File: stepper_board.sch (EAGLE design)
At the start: 59 parts, among them IC1 MCP1703DB, U2 MIC2005A-1YM5, Y1 12 MHz

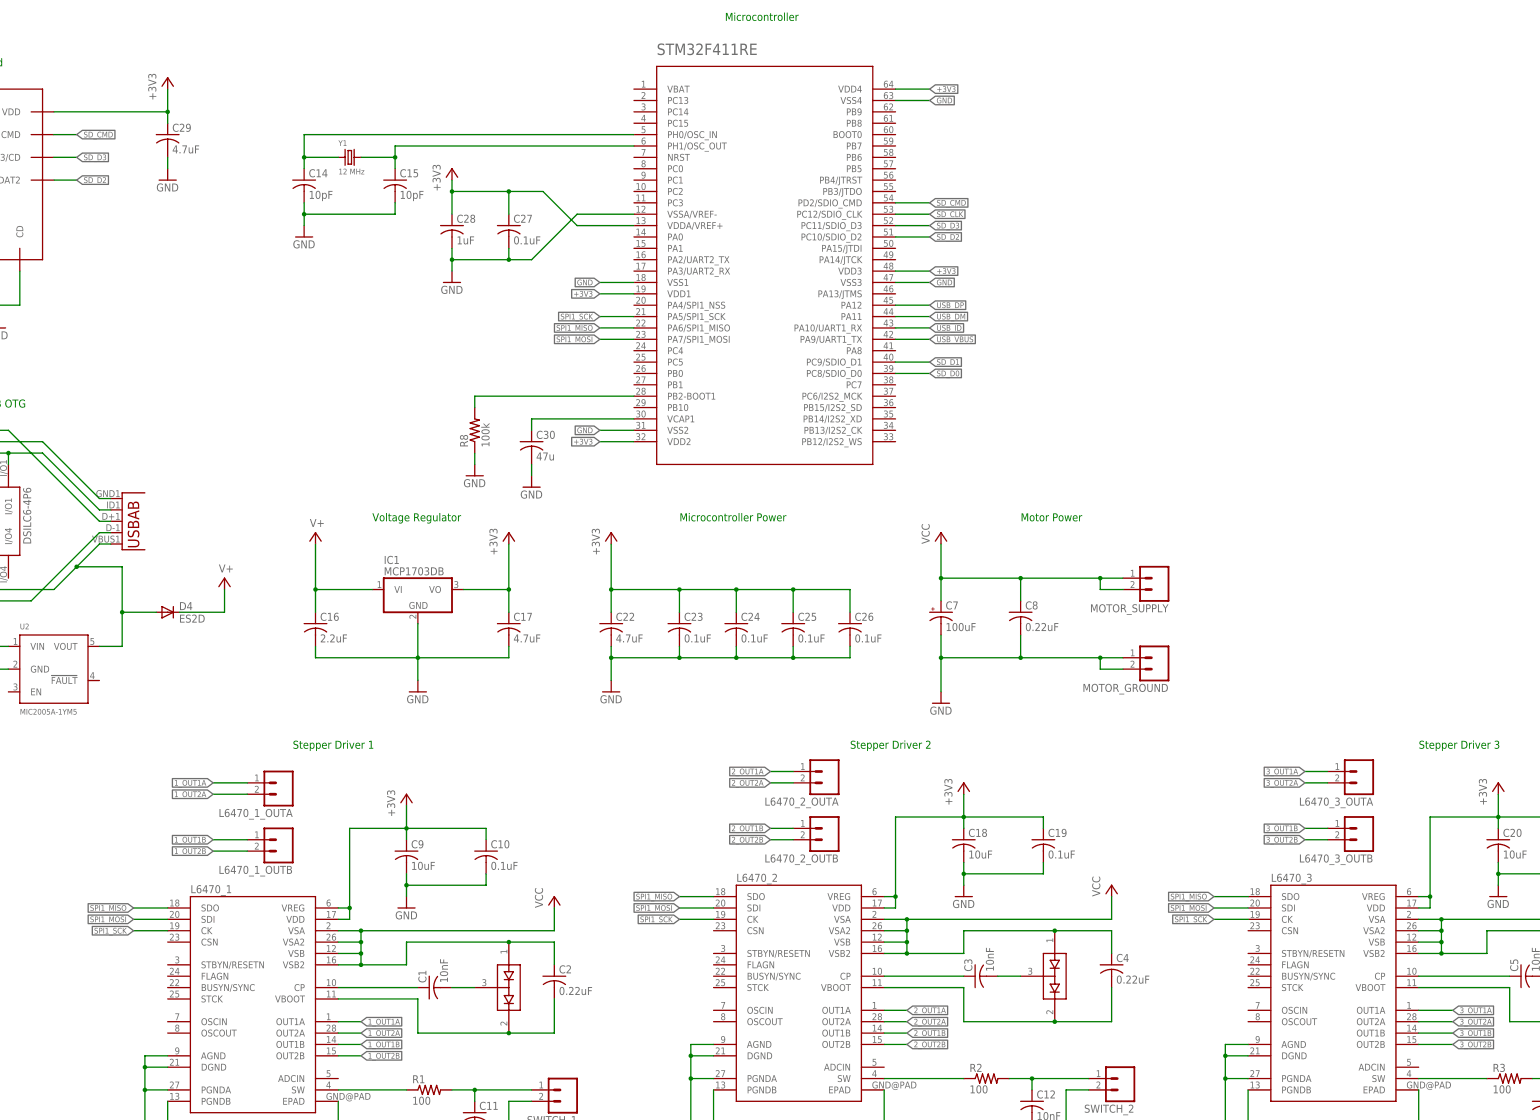
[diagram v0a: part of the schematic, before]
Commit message: Tried to start unraveling the rats' nest.
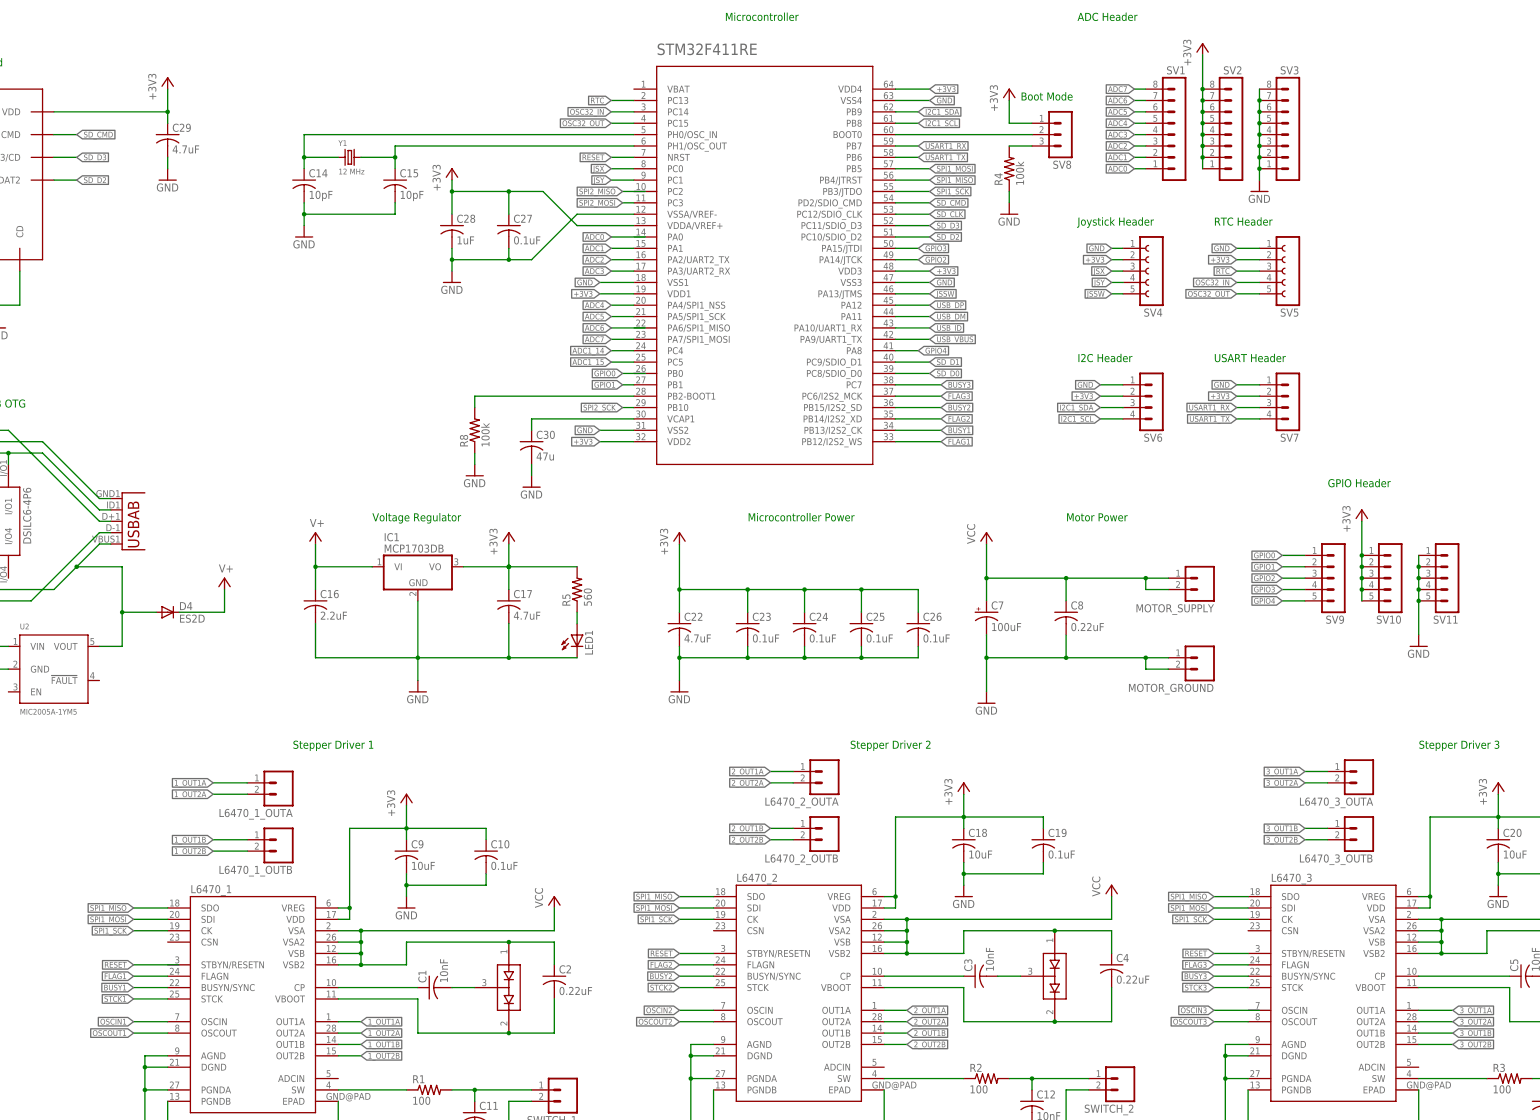
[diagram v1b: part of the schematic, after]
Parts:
- added LED1: (no value), led:LEDCHIP-LED0805
- added R4: 100k, rcl:R-US_R0805
- added R5: 560, rcl:R-US_R0805
- added SV1, SV2, SV3: (no value), con-lstb:MA08-1
- added SV10, SV11, SV9: (no value), con-lstb:MA05-1
- added SV4, SV5: (no value), con-lsta:FE05-1
- added SV6, SV7: (no value), con-lstb:MA04-1
- added SV8: (no value), con-lstb:MA03-1
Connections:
- new net ADC0: SV1.1
- new net ADC1: STM32F411RE.PA1, SV1.2
- new net ADC1_14: STM32F411RE.PC4
- new net ADC1_15: STM32F411RE.PC5
- new net ADC2: STM32F411RE.PA2/UART2_TX, SV1.3
- new net ADC3: STM32F411RE.PA3/UART2_RX, SV1.4
- new net ADC4: STM32F411RE.PA4/SPI1_NSS, SV1.5
- new net ADC5: STM32F411RE.PA5/SPI1_SCK, SV1.6
- new net ADC6: SV1.7
- new net ADC7: STM32F411RE.PA7/SPI1_MOSI, SV1.8
- new net BUSY1: L6470_1.BUSYN/SYNC, STM32F411RE.PB13/I2S2_CK
- new net BUSY2: L6470_2.BUSYN/SYNC, STM32F411RE.PB15/I2S2_SD
- new net BUSY3: L6470_3.BUSYN/SYNC, STM32F411RE.PC7
- new net FLAG1: L6470_1.FLAGN, STM32F411RE.PB12/I2S2_WS
- new net FLAG2: L6470_2.FLAGN, STM32F411RE.PB14/I2S2_XD
- new net FLAG3: L6470_3.FLAGN, STM32F411RE.PC6/I2S2_MCK
- new net GPIO0: SV9.1
- new net GPIO1: STM32F411RE.PB1, SV9.2
- new net GPIO2: STM32F411RE.PA14/JTCK, SV9.3
- new net GPIO3: STM32F411RE.PA15/JTDI, SV9.4
- new net GPIO4: STM32F411RE.PA8, SV9.5
- new net I2C1_SCL: STM32F411RE.PB8, SV6.4
- new net I2C1_SDA: STM32F411RE.PB9, SV6.3
- new net JSSW: STM32F411RE.PA13/JTMS, SV4.5
- new net JSX: STM32F411RE.PC0, SV4.3
- new net JSY: STM32F411RE.PC1, SV4.4
- new net N$18: STM32F411RE.BOOT0, SV8.2
- new net N$19: R4.2, SV8.3
- new net N$20: LED1.A, R5.1
- new net OSC32_IN: STM32F411RE.PC14, SV5.4
- new net OSC32_OUT: STM32F411RE.PC15, SV5.5
- new net OSCIN1: L6470_1.OSCIN
- new net OSCIN2: L6470_2.OSCIN
- new net OSCOUT1: L6470_1.OSCOUT
- new net OSCOUT2: L6470_2.OSCOUT
- new net OSCOUT3: L6470_3.OSCOUT
- new net RESET: L6470_2.STBYN/RESETN, L6470_3.STBYN/RESETN, STM32F411RE.NRST
- new net RTC: STM32F411RE.PC13, SV5.3
- new net SPI2_MOSI: STM32F411RE.PC3
- new net SPI2_SCK: STM32F411RE.PB10
- new net STCK1: L6470_1.STCK
- new net STCK2: L6470_2.STCK
- new net STCK3: L6470_3.STCK
- new net USART1_RX: STM32F411RE.PB7, SV7.3
- new net USART1_TX: STM32F411RE.PB6, SV7.4
- net +3V3: now also R5.2, SV10.1, SV10.2, SV10.3, SV10.4, SV10.5, SV2.1, SV2.2, SV2.3, SV2.4, SV2.5, SV2.6, SV2.7, SV2.8, SV4.2, SV5.2, SV6.2, SV7.2, SV8.1
- net GND: now also LED1.C, R4.1, SV11.1, SV11.2, SV11.3, SV11.4, SV11.5, SV3.1, SV3.2, SV3.3, SV3.4, SV3.5, SV3.6, SV3.7, SV3.8, SV4.1, SV5.1, SV6.1, SV7.1
- net SPI1_MISO: now also STM32F411RE.PB4/JTRST; no longer STM32F411RE.PA6/SPI1_MISO
- net SPI1_MOSI: now also STM32F411RE.PB5; no longer STM32F411RE.PA7/SPI1_MOSI
- net SPI1_SCK: now also STM32F411RE.PB3/JTDO; no longer STM32F411RE.PA5/SPI1_SCK
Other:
- note added: "ADC Header"
- note added: "Boot Mode"
- note added: "GPIO Header"
- note added: "I2C Header"
- note added: "Joystick Header"
- note added: "RTC Header"
- note added: "USART Header"
- moved on the sheet: C16, C17, C22, C23, C24, C25, C26, C7, C8, IC1, MOTOR_GROUND, MOTOR_SUPPLY

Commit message: More wiring in progress
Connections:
- net 3_OUT1A: now also L6470_3_OUTA.2; no longer L6470_3_OUTA.1
- net 3_OUT2A: now also L6470_3_OUTA.1; no longer L6470_3_OUTA.2
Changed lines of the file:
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@@
 </segment>
 <segment>
-<pinref part="L6470_3_OUTA" gate="G$1" pin="1"/>
-<wire x1="127" y1="-111.76" x2="121.92" y2="-111.76" width="0.1524" layer="91"/>
-<label x="121.92" y="-111.76" size="1.27" layer="95" rot="R180" xref="yes"/>
+<pinref part="L6470_3_OUTA" gate="G$1" pin="2"/>
+<wire x1="127" y1="-114.3" x2="121.92" y2="-114.3" width="0.1524" layer="91"/>
+<label x="121.92" y="-114.3" size="1.27" layer="95" rot="R180" xref="yes"/>
 </segment>
 </net>
@@
 </segment>
 <segment>
-<pinref part="L6470_3_OUTA" gate="G$1" pin="2"/>
-<wire x1="127" y1="-114.3" x2="121.92" y2="-114.3" width="0.1524" layer="91"/>
-<label x="121.92" y="-114.3" size="1.27" layer="95" rot="R180" xref="yes"/>
+<pinref part="L6470_3_OUTA" gate="G$1" pin="1"/>
+<wire x1="127" y1="-111.76" x2="121.92" y2="-111.76" width="0.1524" layer="91"/>
+<label x="121.92" y="-111.76" size="1.27" layer="95" rot="R180" xref="yes"/>
 </segment>
 </net>

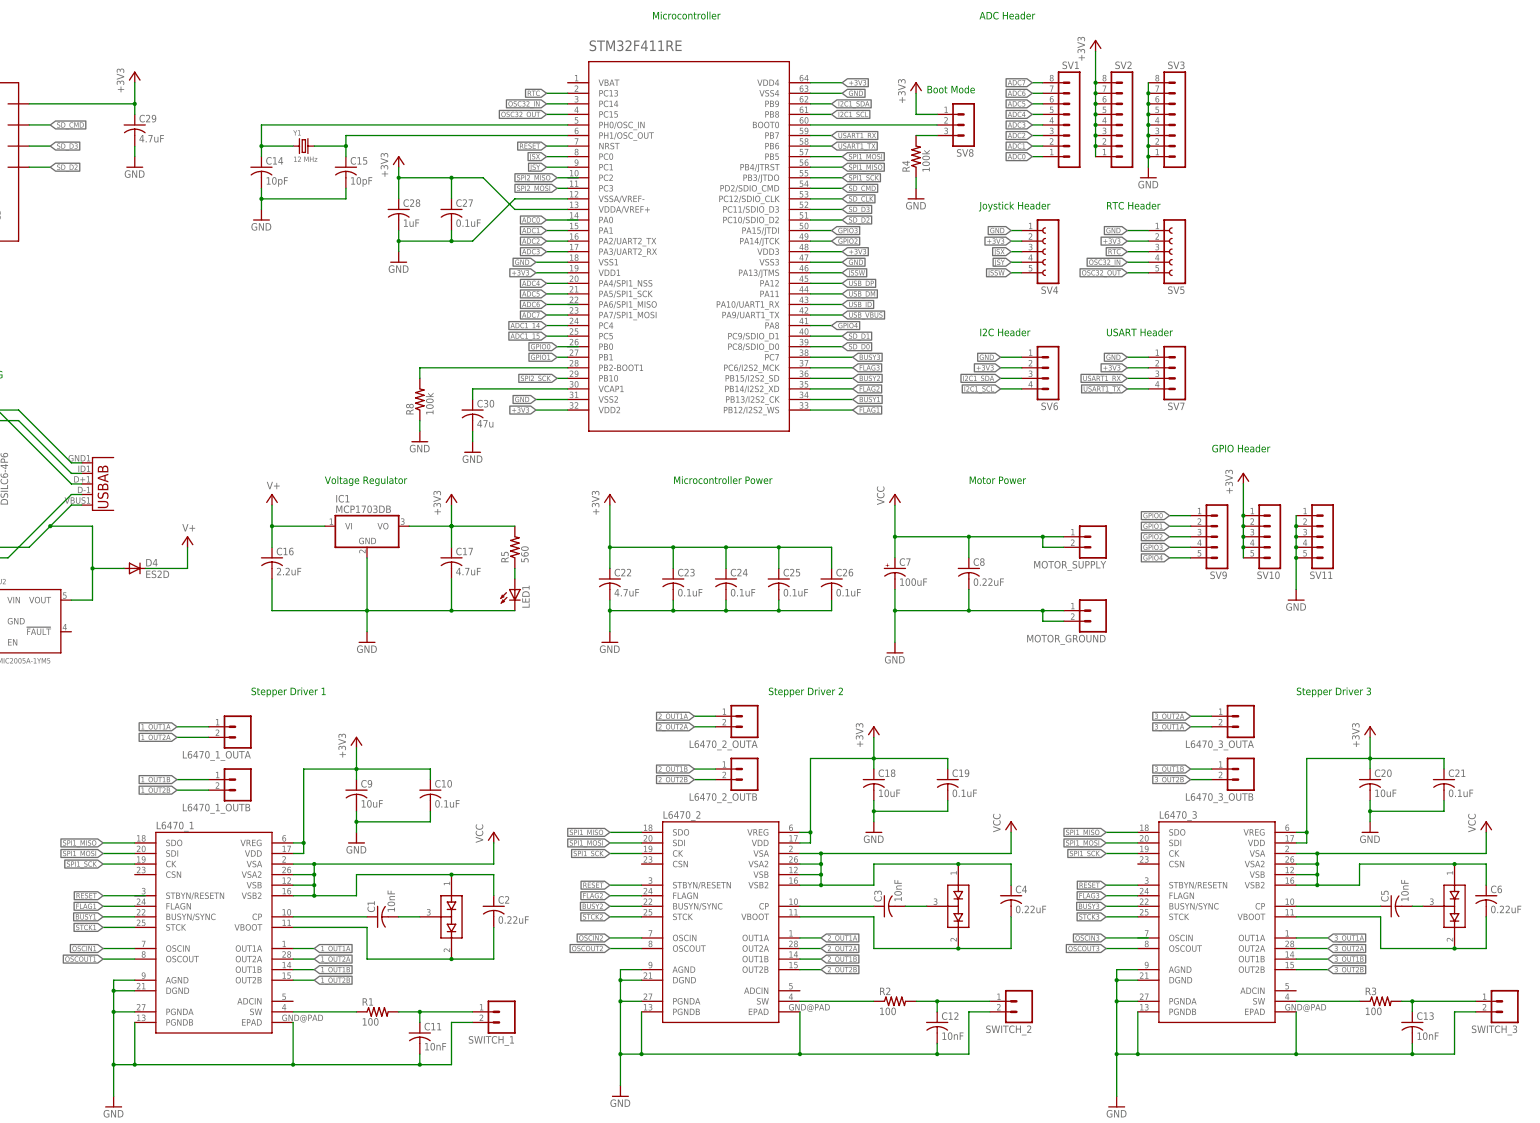
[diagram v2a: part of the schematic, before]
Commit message: Changed L6470 package footprint, added chip select pins to drivers, started routing
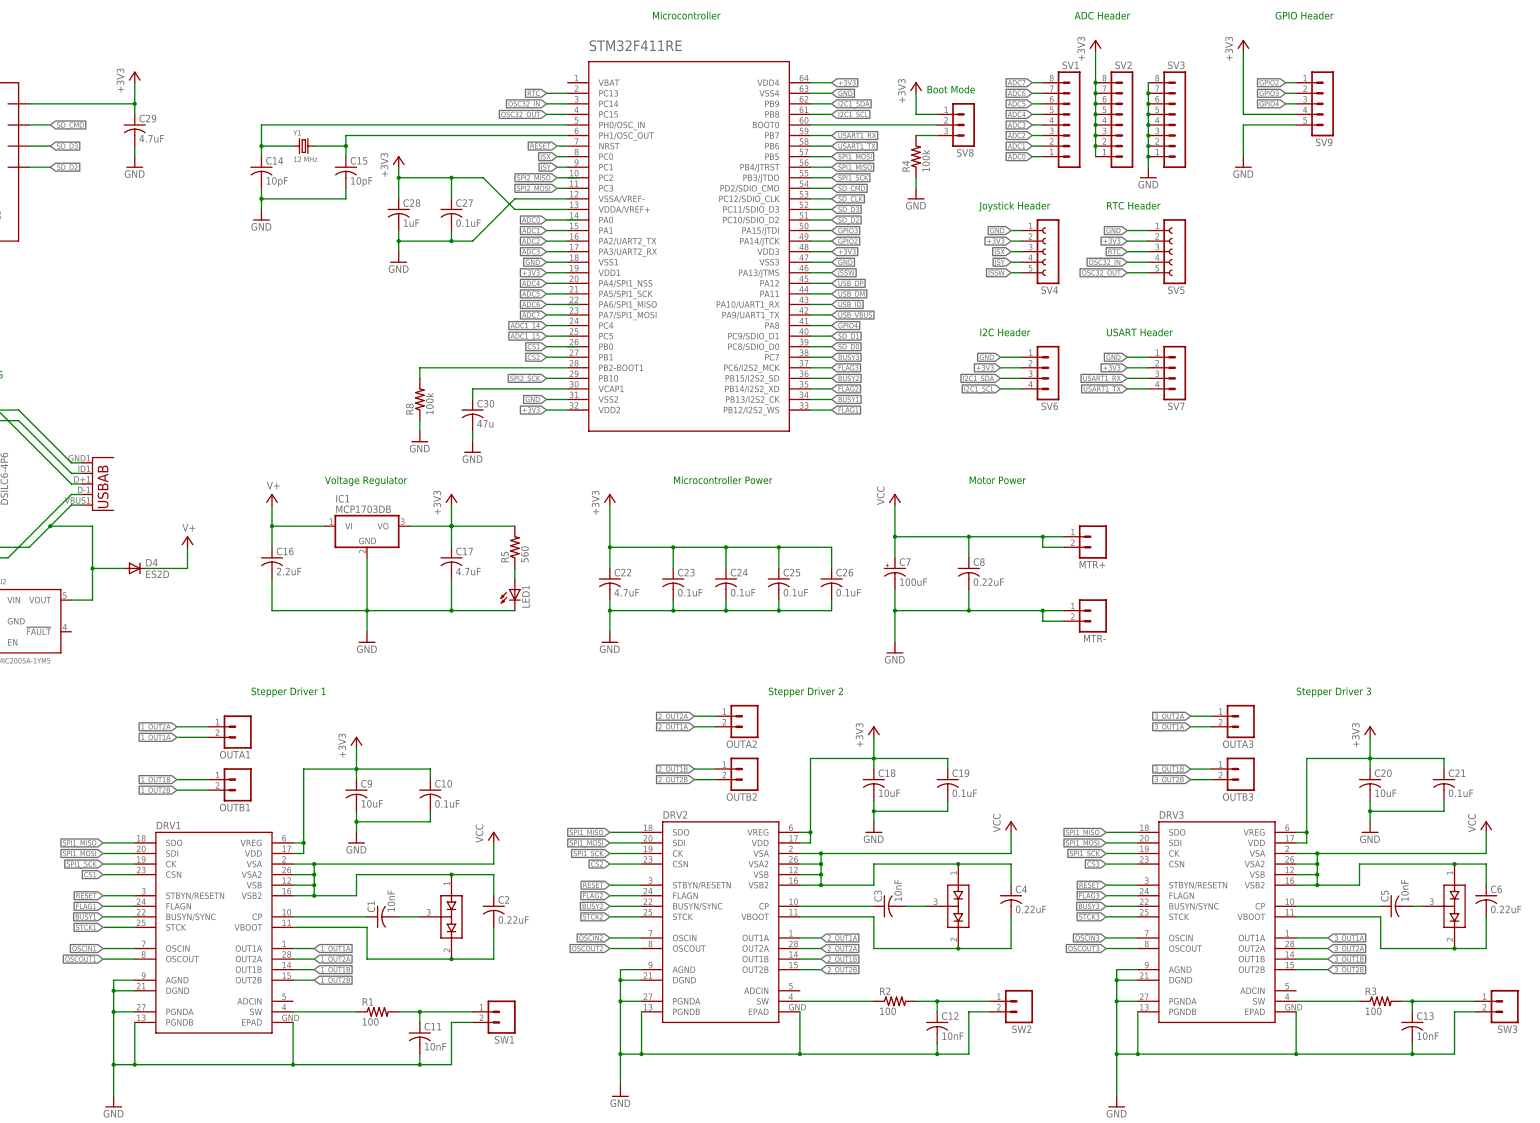
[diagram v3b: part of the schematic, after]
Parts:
- removed L6470_1, L6470_2, L6470_3: (no value), SparkFun-PowerIC:L6470
- removed SV10, SV11: (no value), con-lstb:MA05-1
- added DRV1, DRV2, DRV3: (no value), PowerIC_spark:L6470
- renumbered L6470_1_OUTA to OUTA1, L6470_1_OUTB to OUTB1, L6470_2_OUTA to OUTA2, L6470_2_OUTB to OUTB2, L6470_3_OUTA to OUTA3, L6470_3_OUTB to OUTB3, MOTOR_GROUND to MTR-, MOTOR_SUPPLY to MTR+, SWITCH_1 to SW1, SWITCH_2 to SW2, SWITCH_3 to SW3
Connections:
- removed net GPIO0: SV9.1
- removed net GPIO1: STM32F411RE.PB1, SV9.2
- new net CS1: DRV1.CSN
- new net CS2: DRV2.CSN, STM32F411RE.PB1
- new net CS3: DRV3.CSN
- new net OSCIN3: DRV3.OSCIN
- net +3V3: now also DRV1.VDD, DRV1.VREG, DRV2.VDD, DRV2.VREG, DRV3.VDD, DRV3.VREG, SV9.4; no longer L6470_1.VDD, L6470_1.VREG, L6470_2.VDD, L6470_2.VREG, L6470_3.VDD, L6470_3.VREG, SV10.1, SV10.2, SV10.3, SV10.4, SV10.5
- net 1_OUT1A: now also DRV1.OUT1A, OUTA1.2; no longer L6470_1.OUT1A, OUTA1.1
- net 1_OUT1B: now also DRV1.OUT1B; no longer L6470_1.OUT1B
- net 1_OUT2A: now also DRV1.OUT2A, OUTA1.1; no longer L6470_1.OUT2A, OUTA1.2
- net 1_OUT2B: now also DRV1.OUT2B; no longer L6470_1.OUT2B
- net 2_OUT1A: now also DRV2.OUT1A, OUTA2.2; no longer L6470_2.OUT1A, OUTA2.1
- net 2_OUT1B: now also DRV2.OUT1B; no longer L6470_2.OUT1B
- net 2_OUT2A: now also DRV2.OUT2A, OUTA2.1; no longer L6470_2.OUT2A, OUTA2.2
- net 2_OUT2B: now also DRV2.OUT2B; no longer L6470_2.OUT2B
- net 3_OUT1A: now also DRV3.OUT1A; no longer L6470_3.OUT1A
- net 3_OUT1B: now also DRV3.OUT1B; no longer L6470_3.OUT1B
- net 3_OUT2A: now also DRV3.OUT2A; no longer L6470_3.OUT2A
- net 3_OUT2B: now also DRV3.OUT2B; no longer L6470_3.OUT2B
- net BUSY1: now also DRV1.BUSYN/SYNC; no longer L6470_1.BUSYN/SYNC
- net BUSY2: now also DRV2.BUSYN/SYNC; no longer L6470_2.BUSYN/SYNC
- net BUSY3: now also DRV3.BUSYN/SYNC; no longer L6470_3.BUSYN/SYNC
- net FLAG1: now also DRV1.FLAGN; no longer L6470_1.FLAGN
- net FLAG2: now also DRV2.FLAGN; no longer L6470_2.FLAGN
- net FLAG3: now also DRV3.FLAGN; no longer L6470_3.FLAGN
- net GND: now also DRV1.AGND, DRV1.DGND, DRV1.EPAD, DRV1.PGNDA, DRV1.PGNDB, DRV2.AGND, DRV2.DGND, DRV2.EPAD, DRV2.PGNDA, DRV2.PGNDB, DRV3.AGND, DRV3.DGND, DRV3.EPAD, DRV3.PGNDA, DRV3.PGNDB, SV9.5; no longer L6470_1.AGND, L6470_1.DGND, L6470_1.EPAD, L6470_1.PGNDA, L6470_1.PGNDB, L6470_2.AGND, L6470_2.DGND, L6470_2.EPAD, L6470_2.PGNDA, L6470_2.PGNDB, L6470_3.AGND, L6470_3.DGND, L6470_3.EPAD, L6470_3.PGNDA, L6470_3.PGNDB, SV11.1, SV11.2, SV11.3, SV11.4, SV11.5
- net GPIO2: now also SV9.1; no longer SV9.3
- net GPIO3: now also SV9.2; no longer SV9.4
- net GPIO4: now also SV9.3; no longer SV9.5
- net N$1: now also DRV1.CP; no longer L6470_1.CP
- net N$10: now also DRV3.VBOOT; no longer L6470_3.VBOOT
- net N$12: now also DRV2.SW; no longer L6470_2.SW
- net N$14: now also DRV3.SW; no longer L6470_3.SW
- net N$3: now also DRV1.VBOOT; no longer L6470_1.VBOOT
- net N$4: now also DRV2.CP; no longer L6470_2.CP
- net N$6: now also DRV2.VBOOT; no longer L6470_2.VBOOT
- net N$7: now also DRV1.SW; no longer L6470_1.SW
- net N$8: now also DRV3.CP; no longer L6470_3.CP
- net OSCIN1: now also DRV1.OSCIN; no longer L6470_1.OSCIN
- net OSCIN2: now also DRV2.OSCIN; no longer L6470_2.OSCIN
- net OSCOUT1: now also DRV1.OSCOUT; no longer L6470_1.OSCOUT
- net OSCOUT2: now also DRV2.OSCOUT; no longer L6470_2.OSCOUT
- net OSCOUT3: now also DRV3.OSCOUT; no longer L6470_3.OSCOUT
- net RESET: now also DRV1.STBYN/RESETN, DRV2.STBYN/RESETN, DRV3.STBYN/RESETN; no longer L6470_2.STBYN/RESETN, L6470_3.STBYN/RESETN
- net SPI1_MISO: now also DRV1.SDO, DRV2.SDO, DRV3.SDO; no longer L6470_1.SDO, L6470_2.SDO, L6470_3.SDO
- net SPI1_MOSI: now also DRV1.SDI, DRV2.SDI, DRV3.SDI; no longer L6470_1.SDI, L6470_2.SDI, L6470_3.SDI
- net SPI1_SCK: now also DRV1.CK, DRV2.CK, DRV3.CK; no longer L6470_1.CK, L6470_2.CK, L6470_3.CK
- net STCK1: now also DRV1.STCK; no longer L6470_1.STCK
- net STCK2: now also DRV2.STCK; no longer L6470_2.STCK
- net STCK3: now also DRV3.STCK; no longer L6470_3.STCK
- net VCC: now also DRV1.VSA, DRV1.VSA2, DRV1.VSB, DRV1.VSB2, DRV2.VSA, DRV2.VSA2, DRV2.VSB, DRV2.VSB2, DRV3.VSA, DRV3.VSA2, DRV3.VSB, DRV3.VSB2; no longer L6470_1.VSA, L6470_1.VSA2, L6470_1.VSB, L6470_1.VSB2, L6470_2.VSA, L6470_2.VSA2, L6470_2.VSB, L6470_2.VSB2, L6470_3.VSA, L6470_3.VSA2, L6470_3.VSB, L6470_3.VSB2
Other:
- moved on the sheet: SV9
